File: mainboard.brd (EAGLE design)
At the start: 85.7 x 54 mm, 128 parts, among them X1 FH12-24S-0.5SH, X3 87438-02

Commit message: Updated PCB
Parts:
- added R10, R6, R7, R8, R9: (no value), resistor:R0402
- moved C12 10.8 mm to (3.30, 9.98)
- moved U$6 10.4 mm to (3.17, 7.04)
- moved C17 9.63 mm to (15.2, 3.67), turned to 90 degrees
- moved C11 9.45 mm to (6.10, 8.48)
- moved L1 9.33 mm to (3.05, 4.32), turned to 0 degrees
- moved TP1 3.29 mm to (12.6, 32.4)
- moved TP3 3.29 mm to (10.0, 32.4)
- moved TP5 3.29 mm to (7.49, 32.4)
- moved TP2 3.29 mm to (12.6, 35.0)
- moved TP4 3.29 mm to (10.0, 35.0)
- moved TP6 3.29 mm to (7.49, 35.0)
- moved C6 1.15 mm to (6.65, 12.4)
- moved U$5 1.13 mm to (20.1, 3.80)
- moved C1 0.89 mm to (24.6, 3.70)
- moved C3 0.43 mm to (20.3, 11.0)
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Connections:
- new net BAT_SENS: R6.1, R7.2, U$1.P$25
- new net SD_SWITCH: R8.2, U$1.P$50, U$2.P$10
- net +3V3: now also R10.2, U$2.P$9
- net BOOT0: now also R9.2
- net GND: now also R7.1, R8.1, R9.1
- net NRST: now also R10.1
- net PA13: now also U$1.P$46
- net PA14: now also U$1.P$49
- net VCC: now also R6.2
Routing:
- net SD_SWITCH: track 0.00 -> 113.3 mm
- net NRST: track 22.3 -> 84.6 mm, vias 0 -> 5
- net GND: track 283.8 -> 345.9 mm, vias 15 -> 8
- net KEYROW0: track 93.6 -> 139.3 mm, vias 0 -> 2
- net +3V3: track 142.3 -> 186.1 mm, vias 6 -> 10
- net PA13: track 0.00 -> 24.3 mm, vias 0 -> 6
- net KEYCOL10: track 95.4 -> 119.4 mm
- net KEYROW3: track 161.2 -> 137.9 mm
- net KEYCOL6: track 92.3 -> 72.3 mm, vias 4 -> 5
- net SD_DAT2: track 76.1 -> 95.2 mm, vias 2 -> 0
- net N$54: track 11.0 -> 28.8 mm, vias 2 -> 0
- net KEYROW2: track 103.6 -> 121.3 mm, vias 3 -> 1
- net N$2: track 6.63 -> 24.4 mm
- net KEYCOL2: track 80.4 -> 65.0 mm
- net KEYCOL3: track 71.9 -> 57.4 mm, vias 5 -> 7
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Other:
- outline, holes or cut-outs redrawn

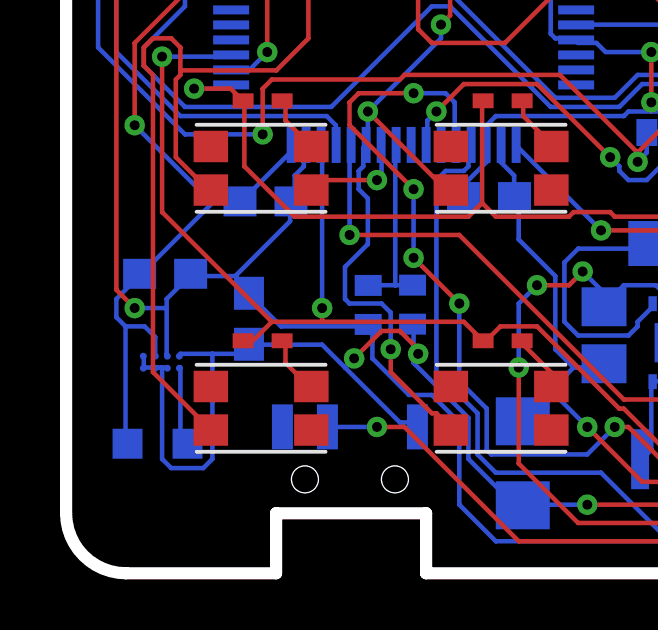
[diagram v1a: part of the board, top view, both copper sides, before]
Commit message: Minor Stetic Modifications
DIN-A4 frame in schematic and relocation.
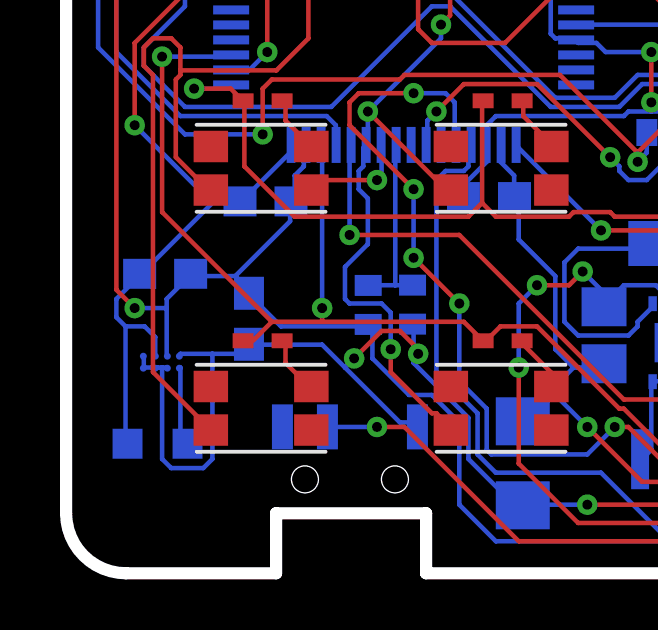
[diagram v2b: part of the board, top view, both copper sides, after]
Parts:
- C1, C12: value (none) -> 10uF
- C11, C2, C3: value (none) -> 4.7uF
- C15, C16: value (none) -> 1uF
- L1: value (none) -> 2.2uH
- R4: value 1k -> <=1.2k
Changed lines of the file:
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@@
 </autorouter>
 <elements>
-<element name="C1" library="resistor" package="C0805" value="" x="24.6294" y="3.7024" smashed="yes" rot="MR180">
+<element name="C1" library="resistor" package="C0805" value="10uF" x="24.6294" y="3.7024" smashed="yes" rot="MR180">
 <attribute name="VALUE" x="23.3594" y="6.2424" size="1.27" layer="28" rot="MR180"/>
 </element>
@@
 <attribute name="VALUE" x="35.2298" y="7.3406" size="1.27" layer="28" rot="MR180"/>
 </element>
-<element name="C2" library="resistor" package="C0805" value="" x="17.931" y="7.9342" smashed="yes" rot="MR270">
+<element name="C2" library="resistor" package="C0805" value="4.7uF" x="17.931" y="7.9342" smashed="yes" rot="MR270">
 <attribute name="VALUE" x="20.471" y="9.2042" size="1.27" layer="28" rot="MR270"/>
 </element>
-<element name="C3" library="resistor" package="C0805" value="" x="20.3394" y="10.9926" smashed="yes" rot="MR180">
+<element name="C3" library="resistor" package="C0805" value="4.7uF" x="20.3394" y="10.9926" smashed="yes" rot="MR180">
 <attribute name="VALUE" x="19.0694" y="13.5326" size="1.27" layer="28" rot="MR180"/>
 </element>
@@
 </element>
 <element name="U$6" library="lib" package="BGA8" value="TPS627431YFPR" x="3.175" y="7.0358" smashed="yes" rot="MR270"/>
-<element name="L1" library="rcl" package="L2012C" value="" x="3.048" y="4.318" smashed="yes" rot="MR0">
+<element name="L1" library="rcl" package="L2012C" value="2.2uH" x="3.048" y="4.318" smashed="yes" rot="MR0">
 <attribute name="VALUE" x="4.953" y="1.778" size="1.27" layer="28" rot="MR0"/>
 </element>
-<element name="C11" library="rcl" package="C0603" value="" x="6.096" y="8.4836" smashed="yes" rot="MR90">
+<element name="C11" library="rcl" package="C0603" value="4.7uF" x="6.096" y="8.4836" smashed="yes" rot="MR90">
 <attribute name="VALUE" x="4.191" y="7.8486" size="1.27" layer="28" rot="MR90"/>
 </element>
-<element name="C12" library="rcl" package="C0603" value="" x="3.302" y="9.9822" smashed="yes" rot="MR180">
+<element name="C12" library="rcl" package="C0603" value="10uF" x="3.302" y="9.9822" smashed="yes" rot="MR180">
 <attribute name="VALUE" x="2.667" y="11.8872" size="1.27" layer="28" rot="MR180"/>
 </element>
@@
 </element>
 <element name="U$8" library="lib" package="6-SOT-23" value="BQ21040DBVR" x="68.4022" y="46.101" smashed="yes" rot="MR270"/>
-<element name="R4" library="resistor" package="R0402" value="1k" x="65.151" y="46.7614" smashed="yes" rot="MR90"/>
+<element name="R4" library="resistor" package="R0402" value="&lt;=1.2k" x="65.151" y="46.7614" smashed="yes" rot="MR90"/>
 <element name="R5" library="resistor" package="R0402" value="10k" x="71.2724" y="47.752" smashed="yes" rot="MR90"/>
-<element name="C15" library="rcl" package="C0603" value="" x="68.1482" y="49.0474" smashed="yes" rot="MR0">
+<element name="C15" library="rcl" package="C0603" value="1uF" x="68.1482" y="49.0474" smashed="yes" rot="MR0">
 <attribute name="VALUE" x="68.7832" y="47.1424" size="1.27" layer="28" rot="MR0"/>
 </element>
-<element name="C16" library="rcl" package="C0603" value="" x="73.406" y="45.3898" smashed="yes" rot="MR90">
+<element name="C16" library="rcl" package="C0603" value="1uF" x="73.406" y="45.3898" smashed="yes" rot="MR90">
 <attribute name="VALUE" x="71.501" y="44.7548" size="1.27" layer="28" rot="MR90"/>
 </element>
@@
 <contactref element="C9" pad="2"/>
 <contactref element="X3" pad="2"/>
-<contactref element="C11" pad="2"/>
-<contactref element="C12" pad="2"/>
-<contactref element="U$6" pad="B2"/>
 <contactref element="U$7" pad="P$2" route="any" routetag="G$1.GND"/>
 <contactref element="U$7" pad="P$4" route="any" routetag="G$1.GND"/>
@@
 <wire x1="3.3528" y1="8.8392" x2="3.3528" y2="7.3152" width="0.1524" layer="16"/>
 <wire x1="4.1148" y1="9.906" x2="3.3528" y2="9.144" width="0.1524" layer="16"/>
-<wire x1="3.3528" y1="7.3152" x2="3.375" y2="7.2358" width="0.1524" layer="16"/>
-<wire x1="4.1148" y1="9.906" x2="4.152" y2="9.9822" width="0.1524" layer="16"/>
 <wire x1="7.1628" y1="8.2296" x2="10.0584" y2="8.2296" width="0.1524" layer="16"/>
 <wire x1="6.096" y1="9.2964" x2="7.1628" y2="8.2296" width="0.1524" layer="16"/>
 <wire x1="10.0584" y1="8.2296" x2="10.0705" y2="8.2951" width="0.1524" layer="16"/>
-<wire x1="6.096" y1="9.2964" x2="6.096" y2="9.3336" width="0.1524" layer="16"/>
 <wire x1="5.6388" y1="9.906" x2="4.2672" y2="9.906" width="0.1524" layer="16"/>
 <wire x1="6.096" y1="9.4488" x2="5.6388" y2="9.906" width="0.1524" layer="16"/>
-<wire x1="4.2672" y1="9.906" x2="4.152" y2="9.9822" width="0.1524" layer="16"/>
-<wire x1="6.096" y1="9.4488" x2="6.096" y2="9.3336" width="0.1524" layer="16"/>
 <wire x1="7.4676" y1="11.7348" x2="7.4676" y2="12.3444" width="0.1524" layer="16"/>
 <wire x1="5.6388" y1="9.906" x2="7.4676" y2="11.7348" width="0.1524" layer="16"/>
@@
 <vertex x="6.985" y="2.0066"/>
 </polygon>
+<contactref element="C11" pad="2"/>
+<contactref element="C12" pad="2"/>
+<contactref element="U$6" pad="B2"/>
 </signal>
 <signal name="+3V3">

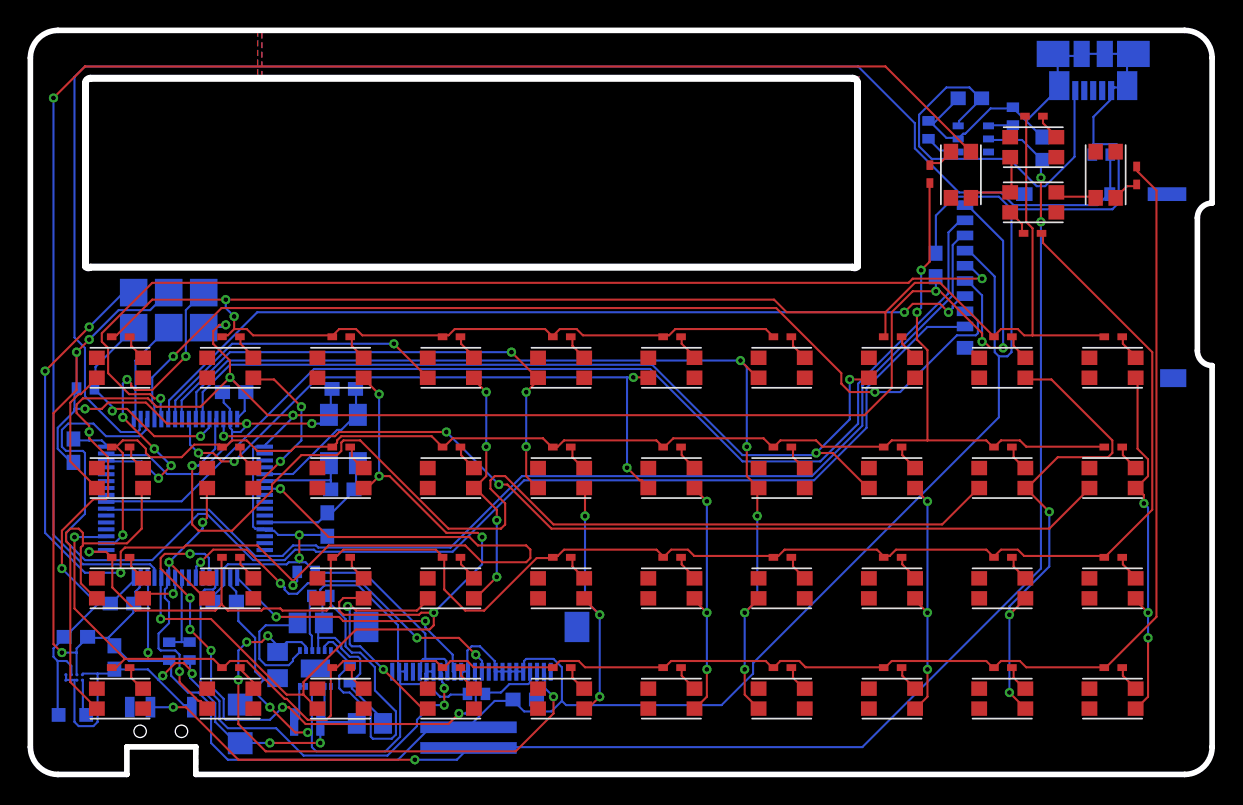
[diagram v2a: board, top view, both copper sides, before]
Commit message: [FIX] Missing EN connection in STOD1317BTPUR
Conected EN Pin in STOD1317BTPUR to 3v3
Added 0402 led for tests.
Moved components from bga8 chip to allow visual inspection of soldering.
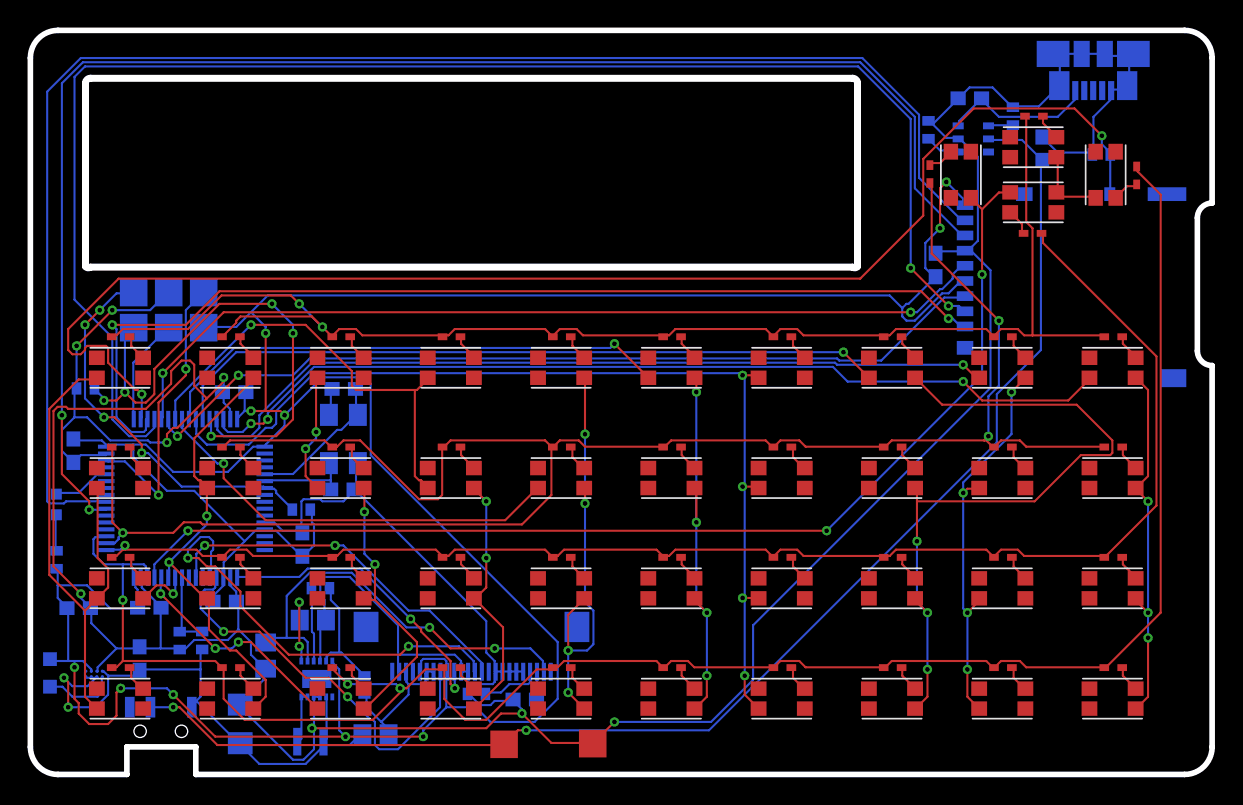
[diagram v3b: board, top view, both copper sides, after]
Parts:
- removed X3: 87438-02, con-molex:87438-02
- added LED1: (no value), eagle-ltspice:LED_SML0603
- added R11: (no value), resistor:R0402
- added TP7, TP8: TPTP20SQ, testpad:TP20SQ
- moved R10 4.54 mm to (19.7, 19.2)
- moved L1 3.45 mm to (1.42, 7.37), turned to 90 degrees
- moved C7 2.31 mm to (19.7, 16.7)
- moved C12 2.09 mm to (3.51, 12.1)
- moved C6 2.00 mm to (8.63, 12.1)
- moved C11 1.83 mm to (7.92, 8.41)
- moved U$6 1.47 mm to (4.62, 7.29)
- moved U$5 1.44 mm to (20.3, 2.38)
- moved R2 1.34 mm to (24.2, 6.49)
- moved R6 1.19 mm to (12.5, 9.72)
- moved C2 1.10 mm to (17.1, 8.62)
- moved R7 1.08 mm to (10.8, 9.71)
- moved C1 0.91 mm to (25.0, 2.89)
- moved U$4 0.77 mm to (20.8, 6.92)
- moved R1 0.56 mm to (21.0, 13.5)
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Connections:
- new net N$57: LED1.A, R11.2
- new net N$58: LED1.C, U$1.P$44
- net +3V3: now also R11.1, U$4.P6
- net GND: now also TP8.TP; no longer X3.2
- net V+: now also TP7.TP; no longer X3.1
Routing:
- net +3V3: track 186.1 -> 242.0 mm
- net NRST: track 84.6 -> 28.7 mm, vias 5 -> 4
- net SD_DAT3: track 72.0 -> 109.0 mm
- net KEYROW0: track 139.3 -> 102.4 mm
- net GND: track 345.5 -> 313.0 mm
- net KEYROW1: track 105.2 -> 137.5 mm
- net KEYCOL10: track 119.4 -> 88.1 mm, vias 1 -> 3
- net SD_DAT0: track 77.3 -> 107.5 mm, vias 0 -> 2
- net SD_DAT1: track 80.6 -> 109.4 mm
- net KEYCOL8: track 116.0 -> 88.7 mm, vias 4 -> 5
- net BOOT0: track 16.6 -> 39.7 mm, vias 2 -> 5
- net KEYCOL7: track 81.0 -> 103.5 mm, vias 5 -> 4
- net SD_DAT2: track 95.2 -> 74.3 mm, vias 0 -> 2
- net KEYCOL2: track 65.0 -> 45.3 mm, vias 5 -> 7
- net N$54: track 28.8 -> 11.3 mm
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- removed copper zone on layer 1, net GND
- removed copper zone on layer 16, net GND
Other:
- board text added: "+"

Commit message: Added Silkscreen
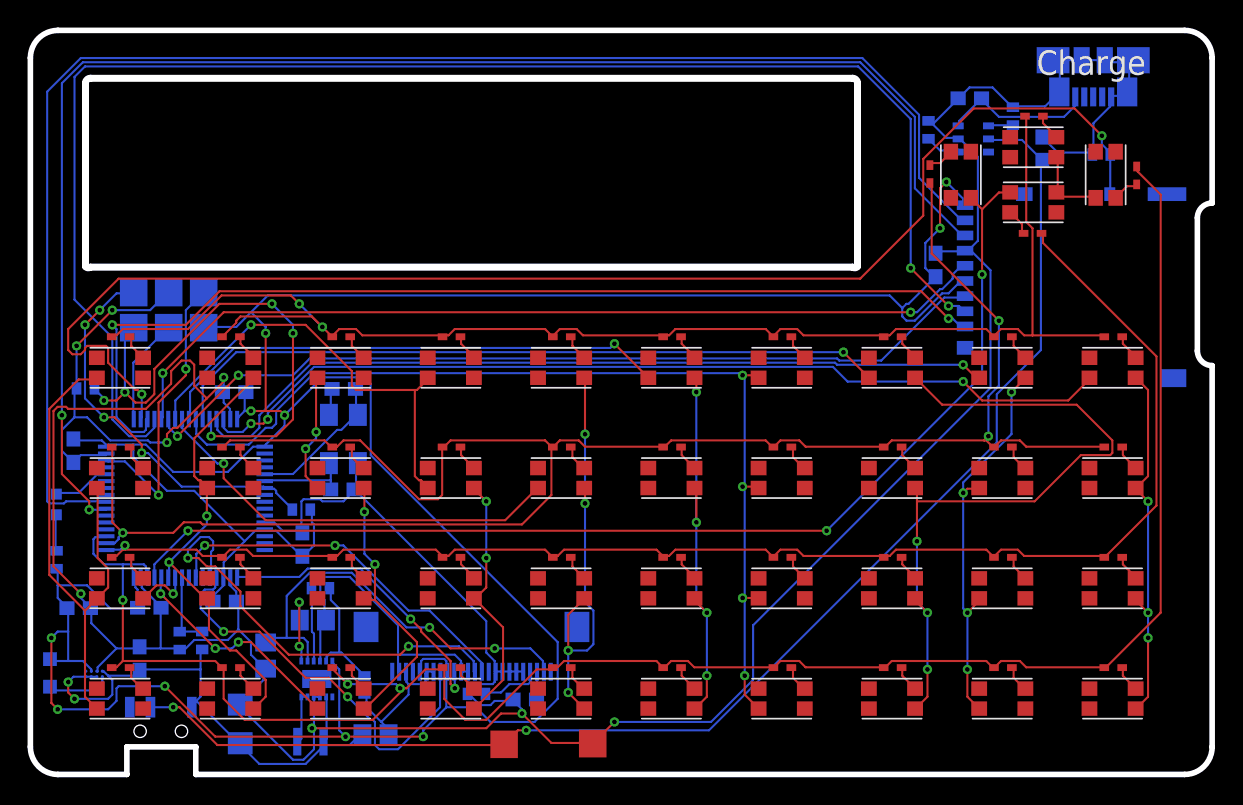
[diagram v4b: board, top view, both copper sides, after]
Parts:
- moved U$3 0.46 mm to (77.1, 51.8)
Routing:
- net +3V3: track 242.0 -> 245.3 mm
- net VCC: track 42.8 -> 39.8 mm
- net N$7: track 5.35 -> 4.52 mm
- net GND: track 313.0 -> 312.4 mm
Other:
- board text added: "Charge"
- board text added: "PA13 | GND | RST 3v3 | PA14 | BOOT"
